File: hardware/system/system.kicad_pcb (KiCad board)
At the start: 2 copper layers, 73.8 x 87.2 mm, 30 parts, among them J1 CART_SOCKET_28P, J2 EXT_PINS, SW1 POWER, SW2 RESET, SW3 A, SW4 B, SW5 UP, SW6 DN, SW7 LF, SW8 RT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

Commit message: Route system board
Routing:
- net Net-(D1-Pad1): track 0.00 -> 152.0 mm
- net Net-(J1-Pad2): track 0.00 -> 123.0 mm
- net VCC: track 0.00 -> 108.8 mm
- net Net-(J1-Pad1): track 0.00 -> 107.4 mm
- net 3V3: track 0.00 -> 102.3 mm, vias 0 -> 1
- net MOSI: track 0.00 -> 75.6 mm, vias 0 -> 1
- net SCK: track 0.00 -> 74.1 mm, vias 0 -> 1
- net Net-(J1-Pad24): track 0.00 -> 65.1 mm
- net Net-(J1-Pad22): track 0.00 -> 61.0 mm, vias 0 -> 1
- net Net-(BZ1-Pad2): track 0.00 -> 55.5 mm
- net Net-(J1-Pad26): track 0.00 -> 54.5 mm
- net Net-(J1-Pad20): track 0.00 -> 49.6 mm, vias 0 -> 1
- net Net-(J1-Pad21): track 0.00 -> 48.9 mm, vias 0 -> 1
- net Net-(J1-Pad7): track 0.00 -> 48.9 mm, vias 0 -> 1
- net D10_A10: track 0.00 -> 45.9 mm
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
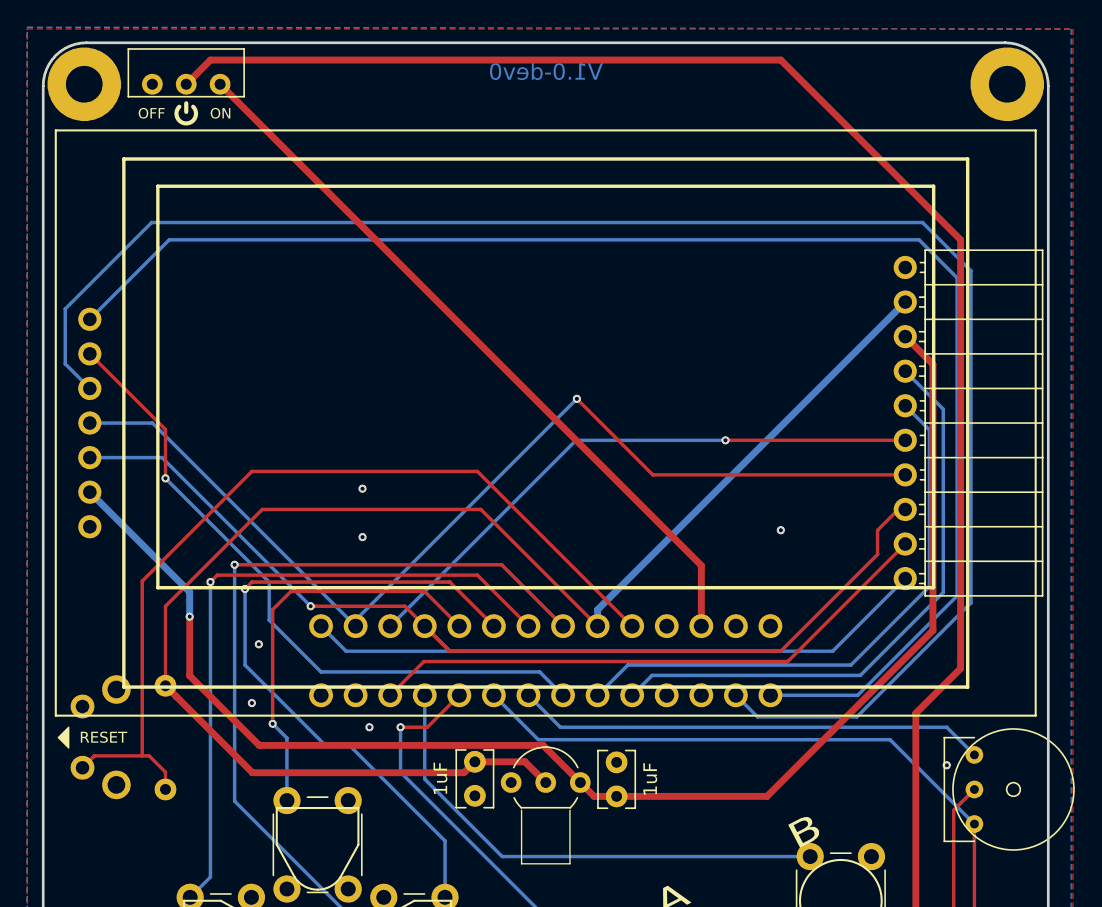
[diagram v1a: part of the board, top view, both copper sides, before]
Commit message: OLED RES -> RST (board), break out RX/D0
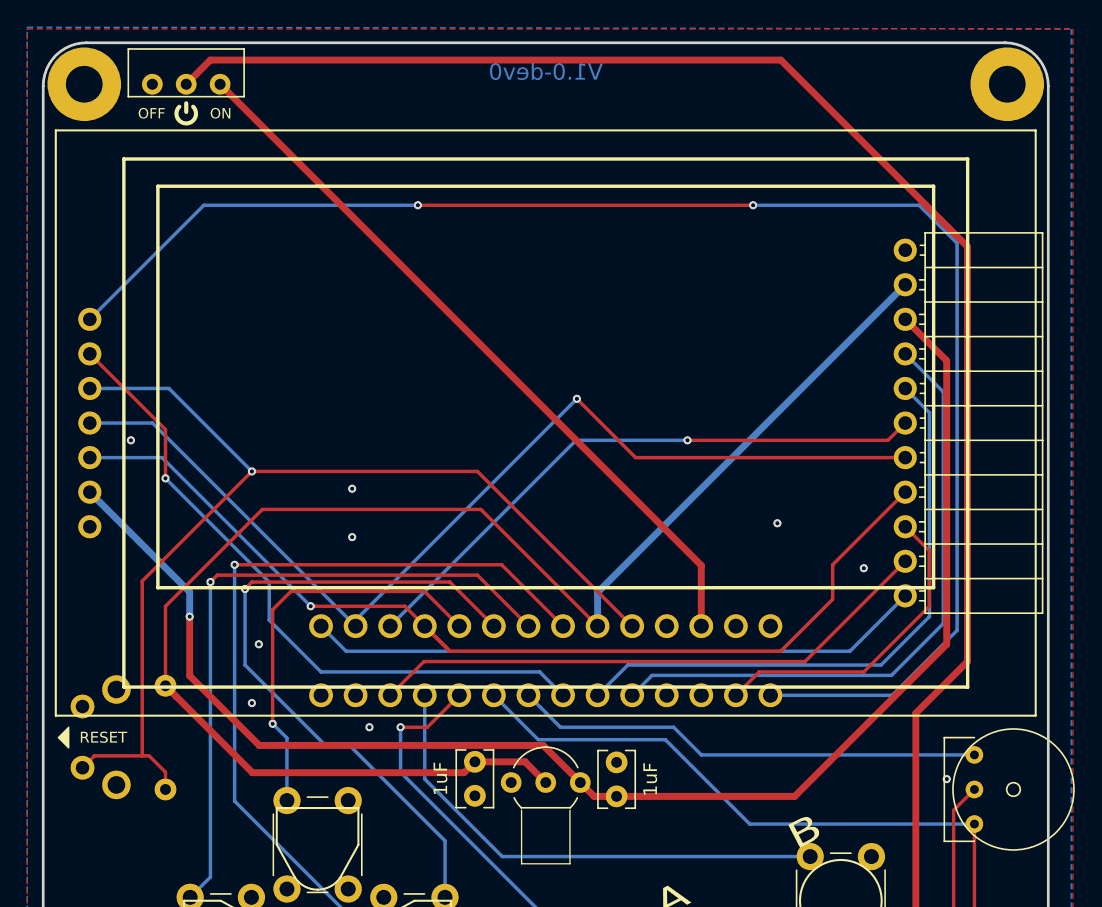
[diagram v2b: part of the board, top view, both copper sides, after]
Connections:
- J1 pad 2: Net-(J1-Pad2) -> D0
- J2 pad 10: D10_A10 -> D9_A9
- J2 pad 9: D9_A9 -> D0
- U3 pad 5: Net-(J1-Pad2) -> Net-(J1-Pad24)
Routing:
- net Net-(J1-Pad2): track 123.0 -> 0.00 mm
- net D0: track 0.00 -> 23.5 mm
- net Net-(J1-Pad24): track 65.1 -> 79.5 mm, vias 0 -> 1
- net Net-(J1-Pad1): track 107.4 -> 112.5 mm, vias 0 -> 2
- net 3V3: track 102.3 -> 105.6 mm
- net SDA: track 43.4 -> 46.0 mm
- net SCL: track 41.7 -> 44.3 mm
- net VCC: track 108.8 -> 110.1 mm
- net SCK: track 74.1 -> 74.7 mm
- net D9_A9: track 42.4 -> 41.9 mm
- net D10_A10: track 45.9 -> 45.4 mm
- net MOSI: track 75.6 -> 75.1 mm
- net MISO: track 43.5 -> 44.0 mm
- net GND: vias 7 -> 9

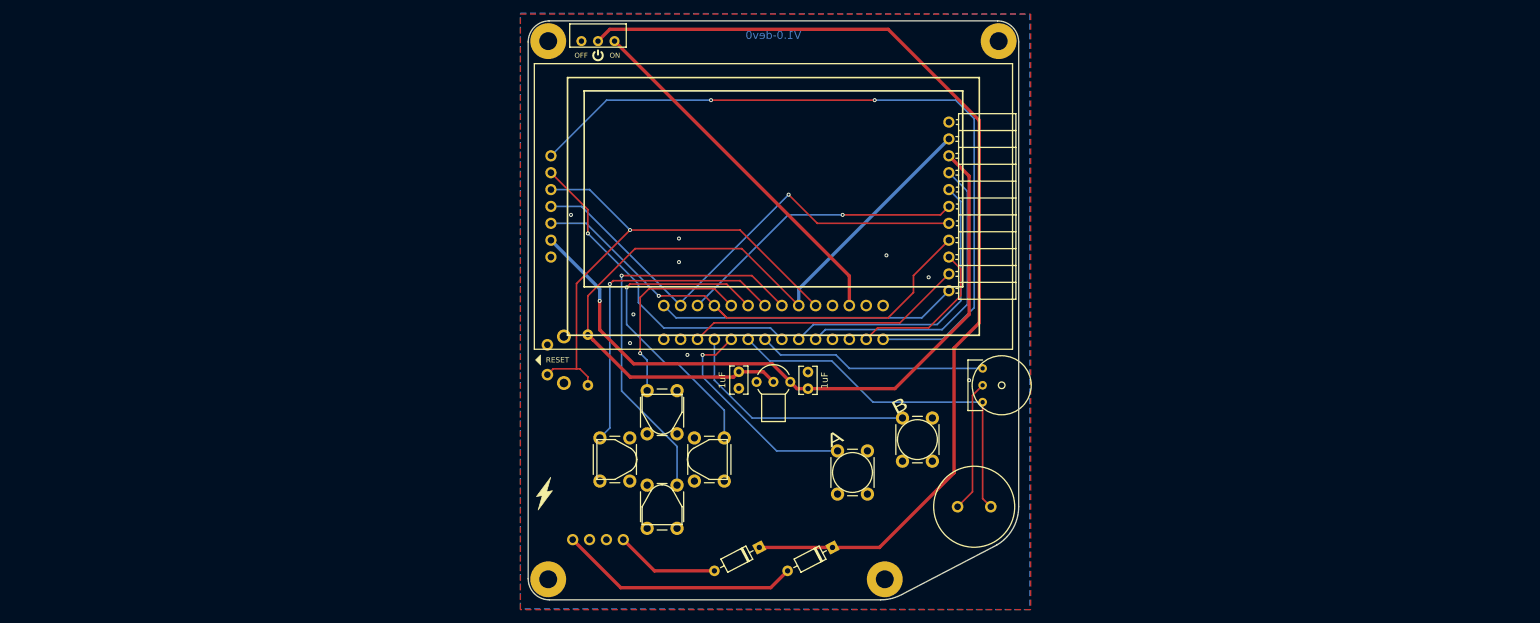
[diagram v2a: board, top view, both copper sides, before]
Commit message: System front/back, extend cart height
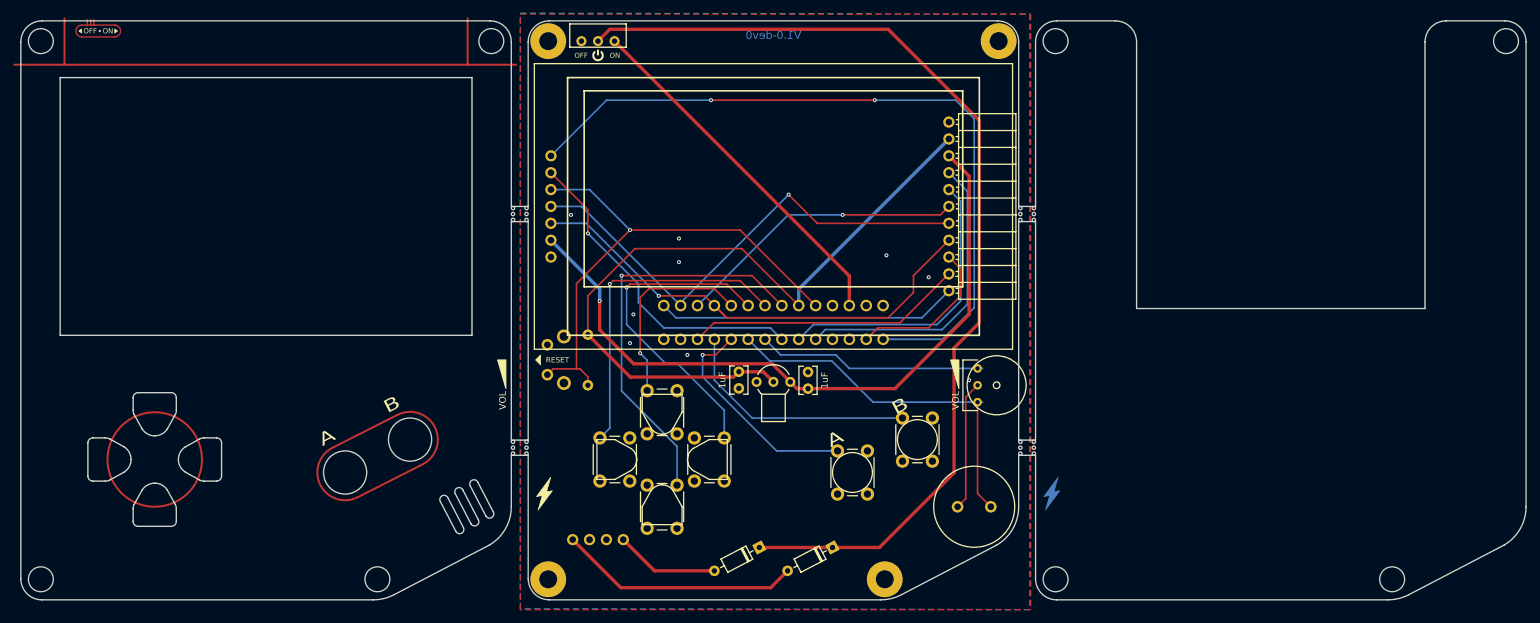
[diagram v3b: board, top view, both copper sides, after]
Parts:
- removed the RV1 at (171.2, 121.9)
- added BZ1: Buzzer, system:BUZZER_CUTOUT, F.Cu at (93.5, 140.2)
- added HOLE: MountingHole_2.7mm_M2.5_Pad, MountingHole:MountingHole_2.7mm_M2.5_Pad, F.Cu at (250.0, 70.1)
- added HOLE: MountingHole_2.7mm_M2.5_Pad, MountingHole:MountingHole_2.7mm_M2.5_Pad, F.Cu at (232.9, 151.1)
- added HOLE: MountingHole_2.7mm_M2.5_Pad, MountingHole:MountingHole_2.7mm_M2.5_Pad, F.Cu at (182.2, 70.1)
- added HOLE: MountingHole_2.7mm_M2.5_Pad, MountingHole:MountingHole_2.7mm_M2.5_Pad, F.Cu at (182.2, 151.1)
- added HOLE: MountingHole_2.7mm_M2.5_Pad, MountingHole:MountingHole_2.7mm_M2.5_Pad, F.Cu at (97.2, 70.1)
- added HOLE: MountingHole_2.7mm_M2.5_Pad, MountingHole:MountingHole_2.7mm_M2.5_Pad, F.Cu at (80.1, 151.1)
- added HOLE: MountingHole_2.7mm_M2.5_Pad, MountingHole:MountingHole_2.7mm_M2.5_Pad, F.Cu at (29.4, 70.1)
- added HOLE: MountingHole_2.7mm_M2.5_Pad, MountingHole:MountingHole_2.7mm_M2.5_Pad, F.Cu at (29.4, 151.1)
- added REF**: OMRON_CAP_B32-2010_CUTOUT, system:OMRON_CAP_B32-2010_CUTOUT, F.Cu at (75.2, 135.1)
- added REF**: BREAKAWAY_TAB, system:BREAKAWAY_TAB, F.Cu at (102.8, 131.3)
- added REF**: OMRON_CAP_B32-2010_CUTOUT, system:OMRON_CAP_B32-2010_CUTOUT, F.Cu at (85.0, 130.1)
- added REF**: OMRON_CAP_B32-2110_CUTOUT, system:OMRON_CAP_B32-2110_CUTOUT, F.Cu at (39.4, 133.1)
- added REF**: OMRON_CAP_B32-2110_CUTOUT, system:OMRON_CAP_B32-2110_CUTOUT, F.Cu at (46.5, 140.2)
- added REF**: OMRON_CAP_B32-2110_CUTOUT, system:OMRON_CAP_B32-2110_CUTOUT, F.Cu at (46.5, 126.0)
- added REF**: OMRON_CAP_B32-2110_CUTOUT, system:OMRON_CAP_B32-2110_CUTOUT, F.Cu at (53.7, 133.1)
- added REF**: BREAKAWAY_TAB, system:BREAKAWAY_TAB, F.Cu at (176.6, 131.3)
- added REF**: BREAKAWAY_TAB, system:BREAKAWAY_TAB, F.Cu at (176.6, 96.1)
- added REF**: BREAKAWAY_TAB, system:BREAKAWAY_TAB, F.Cu at (102.8, 96.1)
- added RV1: VOLUME 10K, system:VOLUME_LABEL, F.Cu at (99.4, 121.9)
- added RV1: VOLUME 10K, system:VOLUME_POT, F.Cu at (170.4, 121.9)
- added U3: SPI_DISPLAY, system:DIYMORE_2.42_IN_OLED_CUTOUT, F.Cu at (63.3, 95.0)
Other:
- board size 73.8 x 87.2 mm -> 226.6 x 87.2 mm
- board text added: "Arduboy CE"
- board text added: "Designed by John, Nathan, and Andrew Meyer"
- board text added: "RESET"
- board text added: "W: 2.9075” H: 3.432”"
- board text added: "github.com/menehune23/arduboy-ce"
